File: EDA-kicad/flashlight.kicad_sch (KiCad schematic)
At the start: 3 parts, among them U5 Flash-LED-Lumiled

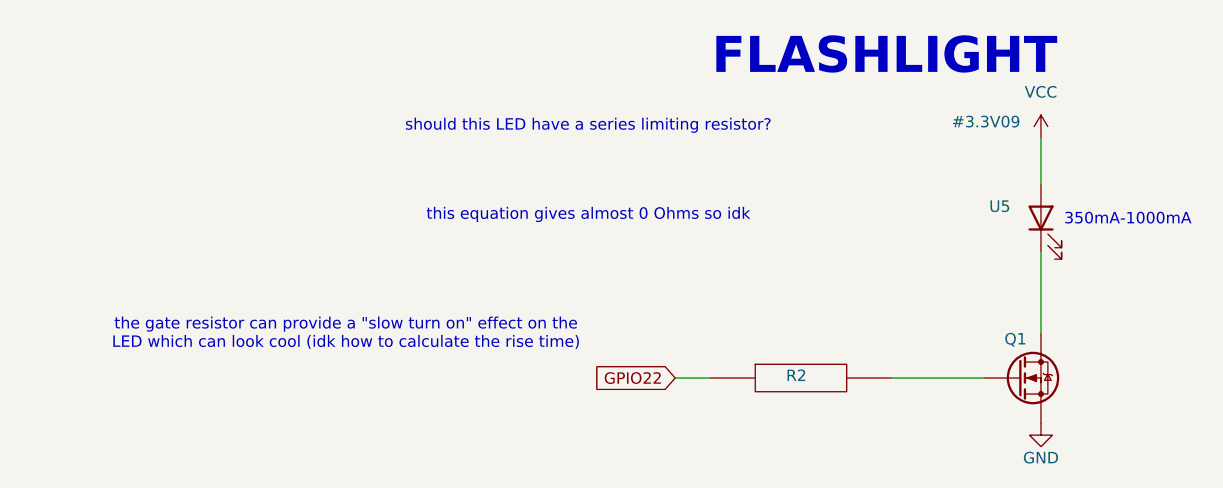
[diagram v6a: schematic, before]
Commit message: reannotate entire schematic
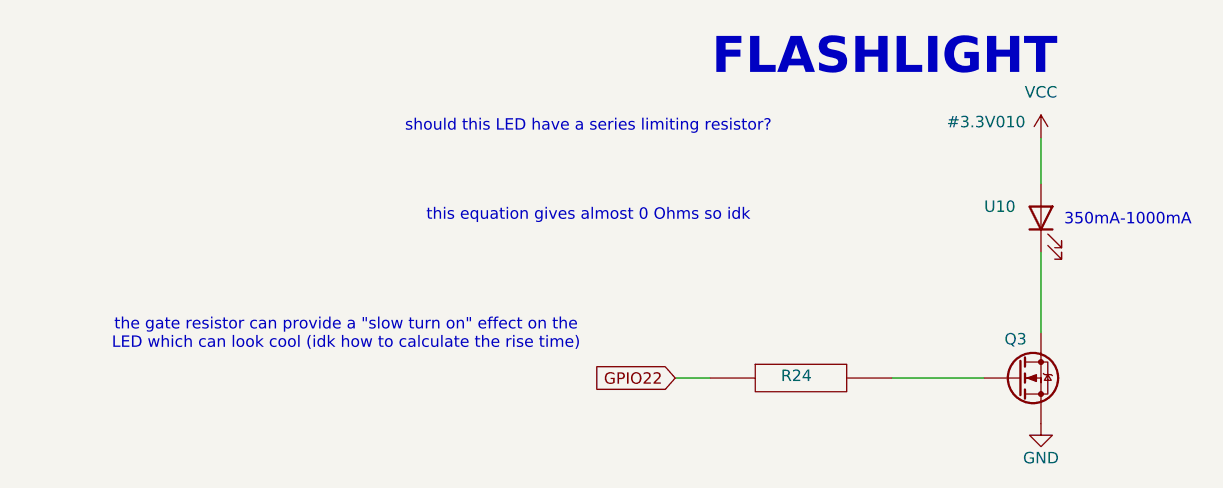
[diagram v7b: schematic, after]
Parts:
- renumbered Q1 to Q3, R2 to R24, U5 to U10
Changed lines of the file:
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@@
+			"AAAAAAAAAAAAAAAAAAAAAAAAAAAAAAAAAAAAAAAAAAAAAAAAAAAAAAAAAAAAAAAAAAAAAAAAAAAA"
+			"AAAAAAAAAAAAAAAAAAAAAAAAAAAAAAAAAAAAAAAAAAAAAAAAAAAAAAAAAAAAAAAAAAAAAAAAAAAA"
+			"AAAAAAAAAAAAAAAAAACQ18ejGX8AAGgrYkdWVQAA6MEeR1ZVAAAHAAAAAAAAAKAgyqMZfwAAcI0f"
+			"R1ZVAABhcmcwAAAAAAAAAAAAAAAAAGAAAAAAAAAAAAAAAAAAAP////8AAAAAAAAAAAAAAAD/////"
+			"//////////8AAAAAAAAAAAAAAAAAAAAAAAAAAAAAAAAAAAAAAAAAAAAAAABQAAAASQAAAHEAAAAA"
+			"AAAA8GCn9FVVAACQr3dHVlUAAEBnHCVWVQAAgMIeR1ZVAAAAAAAAAAAAAGkAAABiAAAAGNrHoxl/"
+			"AAAAAAAAAAAAAAAAAAAAAAAAAgAAAAAAAADgHsqjGX8AALATeEdWVQAAQAEAAAAAAAAgAAAAAAAA"
+			"AJj/exJTVQAAcH1iR1ZVAABgAQAAAAAAACAAAAAAAAAAaCvToFBVAADQHF/6GX8AAIABAAAAAAAA"
+			"kAMAAAAAAAAQhB9HVlUAAAsAAAAAAAAACwAAAAAAAAAAAAAAAAAAAAAAAAAAAAAAAAAAAAAAAAAI"
+			"AAAAAAAAAMBkH0dWVQAABQAAAAAAAAAFAAAAAAAAAAAAAAAAAAAAAAAAAAAAAAAAAAAAAAAAAAQA"
+			"AAAAAAAAkIkfR1ZVAAAyAAAAAAAAADIAAAAAAAAAAAAAAAAAAAAAAAAAAAAAAAAAAAAAAAAABAAA"
+			"AAAAAACgkx9HVlUAAFwAAAAAAAAAXAAAAAAAAAAAAAAAAAAAAAAAAAAAAAAAAAAAAAAAAAAEAAAA"
+			"AAAAAGByH0dWVQAAJAAAAAAAAAAkAAAAAAAAAAAAAAAAAAAAAAAAAAAAAAAAAAAAAAAAAAQAAAAA"
+			"AAAAuI8fR1ZVAAABAAAAAAAAAFEAAAAAAAAAAAAAAAAAAAAAAAAAAAAAAAAAAAAAAAAABAAAAAAA"
+			"AAAglR9HVlUAAAsAAAAAAAAACwAAAAAAAAAAAAAAAAAAAAAAAAAAAAAAAAAAAAAAAAAEAAAAAAAA"
+			"ANCMH0dWVQAABQAAAAAAAAAFAAAAAAAAAAAAAAAAAAAAAAAAAAAAAAAAAAAAAAAAAAEAAAAAAAAA"
+			"IJIfR1ZVAABcAAAAAAAAAFwAAAAAAAAAAAAAAAAAAAAAAAAAAAAAAAAAAAAAAAAAAQAAAAAAAAAA"
+			"lh9HVlUAACQAAAAAAAAAJAAAAAAAAAAAAAAAAAAAAAAAAAAAAAAAAAAAAAAAAAABAAAAAAAAAAAA"
 			"AAAAAAAAAAAAAAAAAAAAAAAAAAAAAAAAAAAAAAAAAAAAAAAAAAAAAAAAAAAAAAAAAAAAAAAAAAAA"
 			"AAAAAAAAAAAAAAAAAAAAAAAAAAAAAAAAAAAAAAAAAAAAAAAAAAAAAAAAAAAAAAAAAAAAAAAAAAAA"
@@
 		(on_board yes)
 		(dnp no)
-		(property "Reference" "U5"
+		(property "Reference" "U10"
 			(at 165.608 85.09 90)
 			(effects
@@
 			(project "cm5-carrier"
 				(path "/28c5e4fe-1ec7-4477-97f0-d2ec1401fad5/b409b5f4-0f84-46c0-84e6-a0b4d149590c"
-					(reference "U5")
+					(reference "U10")
 					(unit 1)
 				)
@@
 		(on_board yes)
 		(dnp no)
-		(property "Reference" "R2"
+		(property "Reference" "R24"
 			(at 143.002 103.886 0)
 			(effects
@@
 			(project "cm5-carrier"
 				(path "/28c5e4fe-1ec7-4477-97f0-d2ec1401fad5/b409b5f4-0f84-46c0-84e6-a0b4d149590c"
-					(reference "R2")
+					(reference "R24")
 					(unit 1)
 				)
@@
 		(on_board yes)
 		(dnp no)
-		(property "Reference" "#3.3V09"
+		(property "Reference" "#3.3V010"
 			(at 164.084 75.692 0)
 			(effects
@@
 			(project "cm5-carrier"
 				(path "/28c5e4fe-1ec7-4477-97f0-d2ec1401fad5/b409b5f4-0f84-46c0-84e6-a0b4d149590c"
-					(reference "#3.3V09")
+					(reference "#3.3V010")
 					(unit 1)
 				)
@@
 		(on_board yes)
 		(dnp no)
-		(property "Reference" "Q1"
+		(property "Reference" "Q3"
 			(at 166.116 99.822 0)
 			(effects
@@
 			(project "cm5-carrier"
 				(path "/28c5e4fe-1ec7-4477-97f0-d2ec1401fad5/b409b5f4-0f84-46c0-84e6-a0b4d149590c"
-					(reference "Q1")
+					(reference "Q3")
 					(unit 1)
 				)
@@
 		(on_board yes)
 		(dnp no)
-		(property "Reference" "#PWR078"
+		(property "Reference" "#PWR0130"
 			(at 170.18 115.57 0)
 			(effects
@@
 			(project "cm5-carrier"
 				(path "/28c5e4fe-1ec7-4477-97f0-d2ec1401fad5/b409b5f4-0f84-46c0-84e6-a0b4d149590c"
-					(reference "#PWR078")
+					(reference "#PWR0130")
 					(unit 1)
 				)

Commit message: add new switches and reannotate
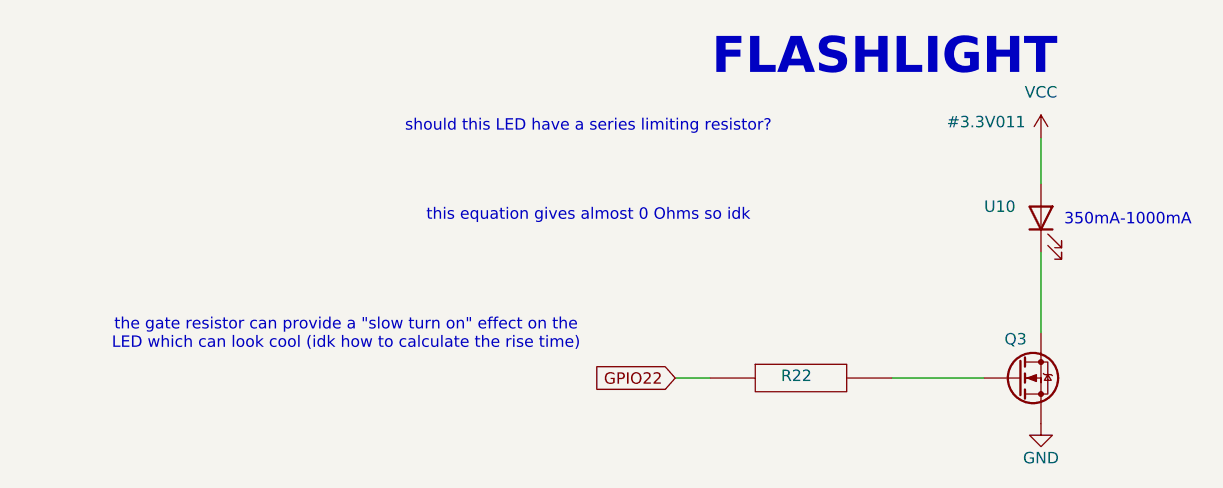
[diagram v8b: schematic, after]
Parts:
- renumbered R24 to R22
